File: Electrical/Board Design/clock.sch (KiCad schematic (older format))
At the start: 21 parts

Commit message: started on schematic capture
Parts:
- removed R? (x3): R, ~, symbol R
- added CON?: AVR-ISP-6, AVR-ISP-6, symbol AVR-ISP-6
- added R? (x3): 10K, ~, symbol R
- R?: value R -> 10K
- RV?: value POT -> 10K
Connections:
- wire segments 64 -> 76
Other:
- note added: "ISP"
- note added: "LIGHTS / BUZZER (EXTRA)"
- note removed: "EXTRAS"
- moved on the sheet: IC?, RV?

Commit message: started into board layout
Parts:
- removed IC?: ATTINY84-M, QFN/MLF20, symbol ATTINY84-M
- removed R? (x2): 10K, ~, symbol R
- removed R? (x2): R, ~, symbol R
- removed RV?: 10K, ~, symbol POT
- removed SW? (x3): SPST, ~, symbol SPST
- added BT1, BT2: BATTERY, ~, symbol BATTERY
- added C1, C3: 10uF, ~, symbol C
- added C5, C6: .01uF, ~, symbol C
- added D1: DIODE, ~, symbol DIODE
- added DS1, DS2: AMMETER, symbol AMMETER
- added IC1: ATTINY84A-SS, SO14, symbol ATTINY84A-SS
- added L1: 4.7uH, ~, symbol INDUCTOR
- added Q1: FET_N, ~, symbol FET_N
- added Q2: FET_P, ~, symbol FET_P
- added R1, R10, R11, R3, R4: 50K, ~, symbol R
- added R13: 220, ~, symbol R
- added R2: 50K, ~, symbol POT
- added R5, R6: R, ~, symbol R
- added S1: QUADRATURE_ENCODR, symbol QUADRATURE_ENCODR
- added SW1: SPST, ~, symbol SPST
- added U1: MCP1624, ~, symbol MCP1624
- C2, C4: renamed from C?; value C -> 12.5pF
- R14, R15: renamed from R?; value R -> 220
- R7, R8: renamed from R?; value R -> 36K
- X1: renamed from X?; value CRYSTAL -> CRYSTAL 32.768kHz
- gave numbers to parts that had none: 6
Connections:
- net labels added: MODE SELECT POWER
- wire segments 76 -> 113
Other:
- note added: "POWER BLOCK"
- moved on the sheet: C2, C4, CON1, D2, D3, R12, R14, R15, R7, R8, R9, SP1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

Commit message: big catchup
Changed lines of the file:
@@
 Sheet 1 1
 Title ""
-Date "18 may 2014"
+Date "22 may 2014"
 Rev ""
 Comp ""
@@
 $EndComp
 Text Label 11300 2700 2    60   ~ 0
+INT 1
+Text Label 7300 2700 0    60   ~ 0
 INT 2
-Text Label 7300 2700 0    60   ~ 0
-INT 1
 Text Notes 7600 1300 0    79   ~ 0
 QUADRATURE ENCODER\nSWITCH DEBOUNCE BLOCK

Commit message: board layout updates for battery stuff
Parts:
- removed BT1, BT2: BATTERY, ~, symbol BATTERY
- added BT1, BT2, BT3, BT4: BATTERY_CLIP, symbol BATTERY_CLIP
- R5: value R -> 130K
- R6: value R -> 200K
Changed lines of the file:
@@
 Sheet 1 1
 Title ""
-Date "22 may 2014"
+Date "8 jul 2014"
 Rev ""
 Comp ""
@@
 $EndDescr
 $Comp
-L GND #PWR18
+L GND #PWR01
 U 1 1 5336447B
 P 10450 3600
-F 0 "#PWR18" H 10450 3600 30  0001 C CNN
+F 0 "#PWR01" H 10450 3600 30  0001 C CNN
 F 1 "GND" H 10450 3530 30  0001 C CNN
 F 2 "" H 10450 3600 60  0000 C CNN
@@
 $EndComp
 $Comp
-L GND #PWR17
+L GND #PWR02
 U 1 1 53364495
 P 9250 3900
-F 0 "#PWR17" H 9250 3900 30  0001 C CNN
+F 0 "#PWR02" H 9250 3900 30  0001 C CNN
 F 1 "GND" H 9250 3830 30  0001 C CNN
 F 2 "" H 9250 3900 60  0000 C CNN
@@
 $EndComp
 $Comp
-L GND #PWR14
+L GND #PWR03
 U 1 1 5336449B
 P 8250 3500
-F 0 "#PWR14" H 8250 3500 30  0001 C CNN
+F 0 "#PWR03" H 8250 3500 30  0001 C CNN
 F 1 "GND" H 8250 3430 30  0001 C CNN
 F 2 "" H 8250 3500 60  0000 C CNN
@@
 $EndComp
 $Comp
-L VCC #PWR16
+L VCC #PWR04
 U 1 1 533644C9
 P 9200 1900
-F 0 "#PWR16" H 9200 2000 30  0001 C CNN
+F 0 "#PWR04" H 9200 2000 30  0001 C CNN
 F 1 "VCC" H 9200 2000 30  0000 C CNN
 F 2 "" H 9200 1900 60  0000 C CNN
@@
 $EndComp
 $Comp
-L GND #PWR15
+L GND #PWR05
 U 1 1 53364820
 P 8500 8400
-F 0 "#PWR15" H 8500 8400 30  0001 C CNN
+F 0 "#PWR05" H 8500 8400 30  0001 C CNN
 F 1 "GND" H 8500 8330 30  0001 C CNN
 F 2 "" H 8500 8400 60  0000 C CNN
@@
 $EndComp
 $Comp
-L GND #PWR13
+L GND #PWR06
 U 1 1 53364C53
 P 6850 9300
-F 0 "#PWR13" H 6850 9300 30  0001 C CNN
+F 0 "#PWR06" H 6850 9300 30  0001 C CNN
 F 1 "GND" H 6850 9230 30  0001 C CNN
 F 2 "" H 6850 9300 60  0000 C CNN
@@
 $EndComp
 $Comp
-L GND #PWR10
+L GND #PWR07
 U 1 1 53364C59
 P 5850 9300
-F 0 "#PWR10" H 5850 9300 30  0001 C CNN
+F 0 "#PWR07" H 5850 9300 30  0001 C CNN
 F 1 "GND" H 5850 9230 30  0001 C CNN
 F 2 "" H 5850 9300 60  0000 C CNN
@@
 $EndComp
 $Comp
-L GND #PWR23
+L GND #PWR08
 U 1 1 53365252
 P 13850 6700
-F 0 "#PWR23" H 13850 6700 30  0001 C CNN
+F 0 "#PWR08" H 13850 6700 30  0001 C CNN
 F 1 "GND" H 13850 6630 30  0001 C CNN
 F 2 "" H 13850 6700 60  0000 C CNN
@@
 $EndComp
 $Comp
-L GND #PWR24
+L GND #PWR09
 U 1 1 53365258
 P 13850 7000
-F 0 "#PWR24" H 13850 7000 30  0001 C CNN
+F 0 "#PWR09" H 13850 7000 30  0001 C CNN
 F 1 "GND" H 13850 6930 30  0001 C CNN
 F 2 "" H 13850 7000 60  0000 C CNN
@@
 $EndComp
 $Comp
-L GND #PWR21
+L GND #PWR010
 U 1 1 53365387
 P 13250 8000
-F 0 "#PWR21" H 13250 8000 30  0001 C CNN
+F 0 "#PWR010" H 13250 8000 30  0001 C CNN
 F 1 "GND" H 13250 7930 30  0001 C CNN
 F 2 "" H 13250 8000 60  0000 C CNN
@@
 LIGHTS / BUZZER (EXTRA)
 $Comp
-L VCC #PWR2
+L VCC #PWR011
 U 1 1 53365427
 P 1700 6150
-F 0 "#PWR2" H 1700 6250 30  0001 C CNN
+F 0 "#PWR011" H 1700 6250 30  0001 C CNN
 F 1 "VCC" H 1700 6250 30  0000 C CNN
 F 2 "" H 1700 6150 60  0000 C CNN
@@
 $EndComp
 $Comp
-L GND #PWR3
+L GND #PWR012
 U 1 1 5336542D
 P 1700 8000
-F 0 "#PWR3" H 1700 8000 30  0001 C CNN
+F 0 "#PWR012" H 1700 8000 30  0001 C CNN
 F 1 "GND" H 1700 7930 30  0001 C CNN
 F 2 "" H 1700 8000 60  0000 C CNN
@@
 MODE SELECT POWER
 $Comp
-L GND #PWR6
+L GND #PWR013
 U 1 1 5373C40E
 P 4250 3050
-F 0 "#PWR6" H 4250 3050 30  0001 C CNN
+F 0 "#PWR013" H 4250 3050 30  0001 C CNN
 F 1 "GND" H 4250 2980 30  0001 C CNN
 F 2 "" H 4250 3050 60  0000 C CNN
@@
 P 5450 2500
 F 0 "R5" V 5530 2500 40  0000 C CNN
-F 1 "R" V 5457 2501 40  0000 C CNN
+F 1 "130K" V 5457 2501 40  0000 C CNN
 F 2 "~" V 5380 2500 30  0000 C CNN
 F 3 "~" H 5450 2500 30  0000 C CNN
@@
 P 5450 3300
 F 0 "R6" V 5530 3300 40  0000 C CNN
-F 1 "R" V 5457 3301 40  0000 C CNN
+F 1 "200K" V 5457 3301 40  0000 C CNN
 F 2 "~" V 5380 3300 30  0000 C CNN
 F 3 "~" H 5450 3300 30  0000 C CNN
@@
 $EndComp
 $Comp
-L GND #PWR11
+L GND #PWR014
 U 1 1 5373C5A4
 P 6050 3100
-F 0 "#PWR11" H 6050 3100 30  0001 C CNN
+F 0 "#PWR014" H 6050 3100 30  0001 C CNN
 F 1 "GND" H 6050 3030 30  0001 C CNN
 F 2 "" H 6050 3100 60  0000 C CNN
@@
 $EndComp
 $Comp
-L VCC #PWR12
+L VCC #PWR015
 U 1 1 5373CA73
 P 6650 2050
-F 0 "#PWR12" H 6650 2150 30  0001 C CNN
+F 0 "#PWR015" H 6650 2150 30  0001 C CNN
 F 1 "VCC" H 6650 2150 30  0000 C CNN
 F 2 "" H 6650 2050 60  0000 C CNN
@@
 $EndComp
 $Comp
-L GND #PWR9
+L GND #PWR016
 U 1 1 5373CA80
 P 5450 3800
-F 0 "#PWR9" H 5450 3800 30  0001 C CNN
+F 0 "#PWR016" H 5450 3800 30  0001 C CNN
 F 1 "GND" H 5450 3730 30  0001 C CNN
 F 2 "" H 5450 3800 60  0000 C CNN
@@
 $EndComp
 $Comp
-L GND #PWR5
+L GND #PWR017
 U 1 1 5373D15F
 P 3100 2950
-F 0 "#PWR5" H 3100 2950 30  0001 C CNN
+F 0 "#PWR017" H 3100 2950 30  0001 C CNN
 F 1 "GND" H 3100 2880 30  0001 C CNN
 F 2 "" H 3100 2950 60  0000 C CNN
@@
 $EndComp
 $Comp
-L BATTERY BT1
-U 1 1 5373D24E
-P 1650 2550
-F 0 "BT1" H 1650 2750 50  0000 C CNN
-F 1 "BATTERY" H 1650 2360 50  0000 C CNN
-F 2 "~" H 1650 2550 60  0000 C CNN
-F 3 "~" H 1650 2550 60  0000 C CNN
-	1    1650 2550
-	0    1    1    0
-$EndComp
-$Comp
-L BATTERY BT2
-U 1 1 5373D25B
-P 2150 2550
-F 0 "BT2" H 2150 2750 50  0000 C CNN
-F 1 "BATTERY" H 2150 2360 50  0000 C CNN
-F 2 "~" H 2150 2550 60  0000 C CNN
-F 3 "~" H 2150 2550 60  0000 C CNN
-	1    2150 2550
-	0    1    1    0
-$EndComp
-$Comp
-L GND #PWR4
+L GND #PWR018
 U 1 1 5373D423
-P 2150 3050
-F 0 "#PWR4" H 2150 3050 30  0001 C CNN
-F 1 "GND" H 2150 2980 30  0001 C CNN
-F 2 "" H 2150 3050 60  0000 C CNN
-F 3 "" H 2150 3050 60  0000 C CNN
-	1    2150 3050
-	1    0    0    -1
-$EndComp
-$Comp
-L GND #PWR1
+P 2150 3700
+F 0 "#PWR018" H 2150 3700 30  0001 C CNN
+F 1 "GND" H 2150 3630 30  0001 C CNN
+F 2 "" H 2150 3700 60  0000 C CNN
+F 3 "" H 2150 3700 60  0000 C CNN
+	1    2150 3700
+	1    0    0    -1
+$EndComp
+$Comp
+L GND #PWR019
 U 1 1 5373D429
-P 1650 3050
-F 0 "#PWR1" H 1650 3050 30  0001 C CNN
-F 1 "GND" H 1650 2980 30  0001 C CNN
-F 2 "" H 1650 3050 60  0000 C CNN
-F 3 "" H 1650 3050 60  0000 C CNN
-	1    1650 3050
+P 1450 3700
+F 0 "#PWR019" H 1450 3700 30  0001 C CNN
+F 1 "GND" H 1450 3630 30  0001 C CNN
+F 2 "" H 1450 3700 60  0000 C CNN
+F 3 "" H 1450 3700 60  0000 C CNN
+	1    1450 3700
 	1    0    0    -1
 $EndComp
@@
 	5450 3550 5450 3800
 Wire Wire Line
-	1650 2050 3700 2050
+	1450 2050 3700 2050
 Wire Wire Line
 	3550 2050 3550 2300
@@
 	3100 2700 3100 2950
 Wire Wire Line
-	1650 2250 1650 2050
+	1450 2250 1450 2050
 Wire Wire Line
 	2150 2250 2150 2050
 Connection ~ 2150 2050
 Wire Wire Line
-	1650 2850 1650 3050
-Wire Wire Line
-	2150 2850 2150 3050
+	1450 3500 1450 3700
+Wire Wire Line
+	2150 3500 2150 3700
 Wire Wire Line
 	10100 2650 10450 2650
@@
 Connection ~ 12700 1900
 $Comp
-L GND #PWR19
+L GND #PWR020
 U 1 1 537512F1
 P 12700 4700
-F 0 "#PWR19" H 12700 4700 30  0001 C CNN
+F 0 "#PWR020" H 12700 4700 30  0001 C CNN
 F 1 "GND" H 12700 4630 30  0001 C CNN
 F 2 "" H 12700 4700 60  0000 C CNN
@@
 	15150 4500 15150 4700
 $Comp
-L GND #PWR22
+L GND #PWR021
 U 1 1 537516B3
 P 13750 4700
-F 0 "#PWR22" H 13750 4700 30  0001 C CNN
+F 0 "#PWR021" H 13750 4700 30  0001 C CNN
 F 1 "GND" H 13750 4630 30  0001 C CNN
 F 2 "" H 13750 4700 60  0000 C CNN
@@
 $EndComp
 $Comp
-L GND #PWR25
+L GND #PWR022
 U 1 1 537516B9
 P 15150 4700
-F 0 "#PWR25" H 15150 4700 30  0001 C CNN
+F 0 "#PWR022" H 15150 4700 30  0001 C CNN
 F 1 "GND" H 15150 4630 30  0001 C CNN
 F 2 "" H 15150 4700 60  0000 C CNN
@@
 	13000 8100 13000 8200
 $Comp
-L GND #PWR20
+L GND #PWR023
 U 1 1 53764BAE
 P 13000 8200
-F 0 "#PWR20" H 13000 8200 30  0001 C CNN
+F 0 "#PWR023" H 13000 8200 30  0001 C CNN
 F 1 "GND" H 13000 8130 30  0001 C CNN
 F 2 "" H 13000 8200 60  0000 C CNN
@@
 	5250 9800 5250 9900
 $Comp
-L GND #PWR8
+L GND #PWR024
 U 1 1 53777472
 P 5250 9900
-F 0 "#PWR8" H 5250 9900 30  0001 C CNN
+F 0 "#PWR024" H 5250 9900 30  0001 C CNN
 F 1 "GND" H 5250 9830 30  0001 C CNN
 F 2 "" H 5250 9900 60  0000 C CNN
@@
 $EndComp
 $Comp
-L VCC #PWR7
+L VCC #PWR025
 U 1 1 5377747A
 P 5250 9500
-F 0 "#PWR7" H 5250 9600 30  0001 C CNN
+F 0 "#PWR025" H 5250 9600 30  0001 C CNN
 F 1 "VCC" H 5250 9600 30  0000 C CNN
 F 2 "" H 5250 9500 60  0000 C CNN
@@
 	1    0    0    -1
 $EndComp
+$Comp
+L BATTERY_CLIP BT3
+U 1 1 53B41CA4
+P 2150 2550
+F 0 "BT3" H 2250 2650 60  0000 L CNN
+F 1 "BATTERY_CLIP" H 2250 2750 60  0000 L CNN
+F 2 "" H 2250 2700 60  0000 C CNN
+F 3 "" H 2250 2700 60  0000 C CNN
+	1    2150 2550
+	1    0    0    -1
+$EndComp
+$Comp
+L BATTERY_CLIP BT1
+U 1 1 53B41CBB
+P 1450 2550
+F 0 "BT1" H 800 2650 60  0000 L CNN
+F 1 "BATTERY_CLIP" H 800 2750 60  0000 L CNN
+F 2 "" H 1550 2700 60  0000 C CNN
+F 3 "" H 1550 2700 60  0000 C CNN
+	1    1450 2550
+	1    0    0    -1
+$EndComp
+$Comp
+L BATTERY_CLIP BT2
+U 1 1 53B41CFA
+P 1450 3200
+F 0 "BT2" H 1950 3550 60  0000 L CNN
+F 1 "BATTERY_CLIP" H 1500 3450 60  0000 L CNN
+F 2 "" H 1550 3350 60  0000 C CNN
+F 3 "" H 1550 3350 60  0000 C CNN
+	1    1450 3200
+	-1   0    0    1
+$EndComp
+$Comp
+L BATTERY_CLIP BT4
+U 1 1 53B41D0A
+P 2150 3200
+F 0 "BT4" H 1950 3500 60  0000 L CNN
+F 1 "BATTERY_CLIP" H 1500 3400 60  0000 L CNN
+F 2 "" H 2250 3350 60  0000 C CNN
+F 3 "" H 2250 3350 60  0000 C CNN
+	1    2150 3200
+	-1   0    0    1
+$EndComp
 $EndSCHEMATC

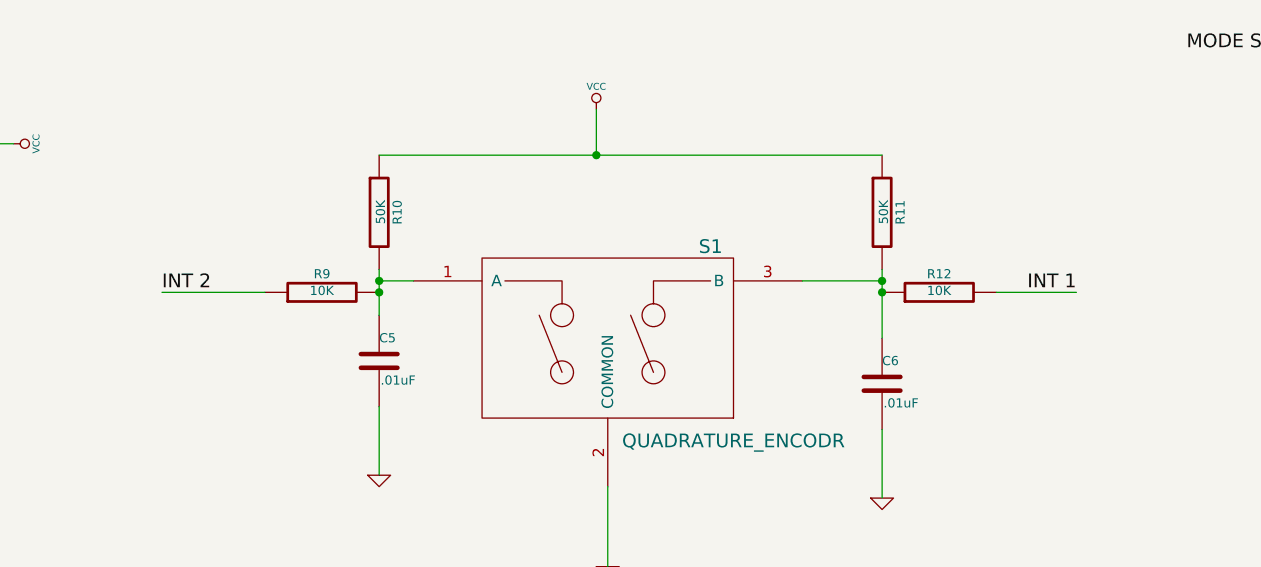
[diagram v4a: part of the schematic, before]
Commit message: updates to board layout
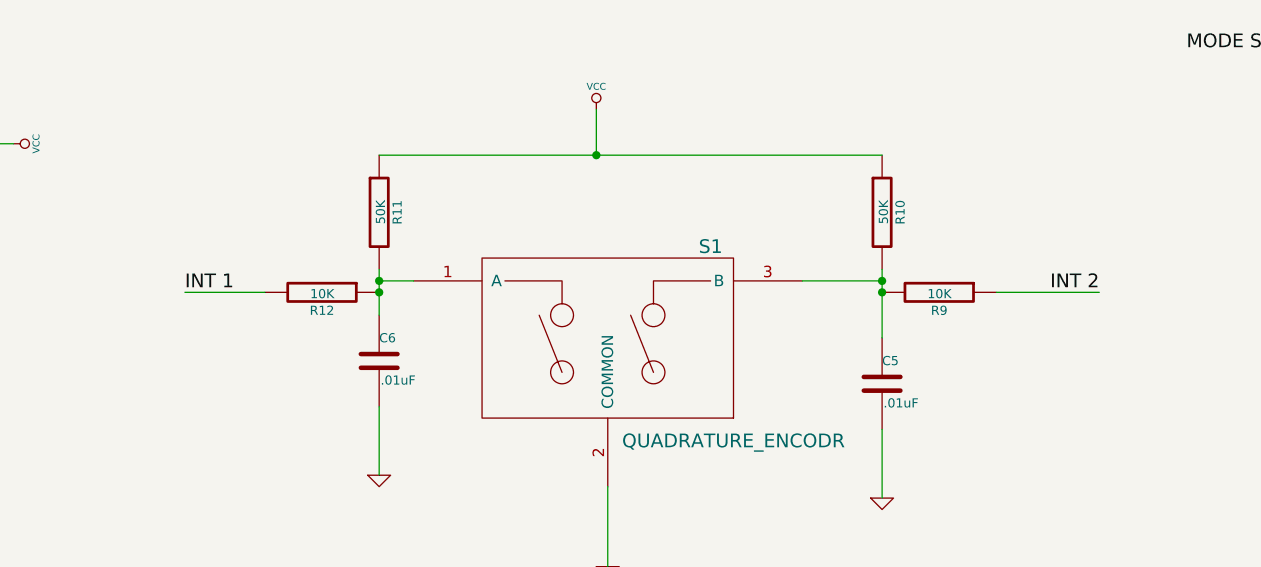
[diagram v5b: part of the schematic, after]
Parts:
- renumbered C6 to C5, C5 to C6, R11 to R10, R10 to R11, R9 to R12, R12 to R9
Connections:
- net INT 1: now also R12.2; no longer R9.2
- net INT 2: now also R9.1; no longer R12.1
- net at C5.1, R10.2, S1.3 (B): now also R9.2; no longer R9.1
- net at C6.1, R11.2, S1.1 (A): now also R12.1; no longer R12.2
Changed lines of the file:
@@
 Sheet 1 1
 Title ""
-Date "8 jul 2014"
+Date "16 jul 2014"
 Rev ""
 Comp ""
@@
 	1    0    0    -1
 $EndComp
-Text Label 11300 2700 2    60   ~ 0
+Text Label 11400 2700 2    60   ~ 0
+INT 2
+Text Label 7400 2700 0    60   ~ 0
 INT 1
-Text Label 7300 2700 0    60   ~ 0
-INT 2
 Text Notes 7600 1300 0    79   ~ 0
 QUADRATURE ENCODER\nSWITCH DEBOUNCE BLOCK
@@
 ISP
 $Comp
-L R R12
+L R R9
 U 1 1 53378721
 P 10700 2700
-F 0 "R12" V 10780 2700 40  0000 C CNN
+F 0 "R9" V 10780 2700 40  0000 C CNN
 F 1 "10K" V 10707 2701 40  0000 C CNN
 F 2 "~" V 10630 2700 30  0000 C CNN
 F 3 "~" H 10700 2700 30  0000 C CNN
 	1    10700 2700
-	0    -1   -1   0
-$EndComp
-$Comp
-L R R9
+	0    1    1    0
+$EndComp
+$Comp
+L R R12
 U 1 1 53378727
 P 8000 2700
-F 0 "R9" V 8080 2700 40  0000 C CNN
+F 0 "R12" V 8080 2700 40  0000 C CNN
 F 1 "10K" V 8007 2701 40  0000 C CNN
 F 2 "~" V 7930 2700 30  0000 C CNN
 F 3 "~" H 8000 2700 30  0000 C CNN
 	1    8000 2700
-	0    -1   -1   0
-$EndComp
-$Comp
-L C C5
+	0    1    1    0
+$EndComp
+$Comp
+L C C6
 U 1 1 536A4944
 P 8250 3000
-F 0 "C5" H 8250 3100 40  0000 L CNN
+F 0 "C6" H 8250 3100 40  0000 L CNN
 F 1 ".01uF" H 8256 2915 40  0000 L CNN
 F 2 "~" H 8288 2850 30  0000 C CNN
@@
 $EndComp
 $Comp
-L C C6
+L C C5
 U 1 1 536A5550
 P 10450 3100
-F 0 "C6" H 10450 3200 40  0000 L CNN
+F 0 "C5" H 10450 3200 40  0000 L CNN
 F 1 ".01uF" H 10456 3015 40  0000 L CNN
 F 2 "~" H 10488 2950 30  0000 C CNN
@@
 	10450 2600 10450 2900
 Connection ~ 8250 2650
-Wire Wire Line
-	10950 2700 11300 2700
 Connection ~ 10450 2700
 Wire Wire Line
@@
 	6600 8600 6850 8600
 Connection ~ 6850 8600
-Wire Wire Line
-	7750 2700 7300 2700
 Connection ~ 8250 2700
 Connection ~ 10450 2650
@@
 $EndComp
 $Comp
-L R R10
+L R R11
 U 1 1 5376426B
 P 8250 2350
-F 0 "R10" V 8330 2350 40  0000 C CNN
+F 0 "R11" V 8330 2350 40  0000 C CNN
 F 1 "50K" V 8257 2351 40  0000 C CNN
 F 2 "~" V 8180 2350 30  0000 C CNN
@@
 $EndComp
 $Comp
-L R R11
+L R R10
 U 1 1 53764271
 P 10450 2350
-F 0 "R11" V 10530 2350 40  0000 C CNN
+F 0 "R10" V 10530 2350 40  0000 C CNN
 F 1 "50K" V 10457 2351 40  0000 C CNN
 F 2 "~" V 10380 2350 30  0000 C CNN
@@
 	-1   0    0    1
 $EndComp
+Wire Wire Line
+	10950 2700 11400 2700
+Wire Wire Line
+	7400 2700 7750 2700
 $EndSCHEMATC
